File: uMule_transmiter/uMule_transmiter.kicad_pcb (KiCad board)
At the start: 2 copper layers, 61 x 69.9 mm, 73 parts, among them J1 Screw_Terminal_01x02, J2 Conn_01x01_Socket, J3 Screw_Terminal_01x02, J4 Conn_01x01_Socket, J5 Test_Point_Sin_I, J6 Test_Point_Sin_O, J7 Test_Point_Cos_I, J8 Test_Point_Cos_O, J9 Screw_Terminal_01x02, U1 TPS61042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

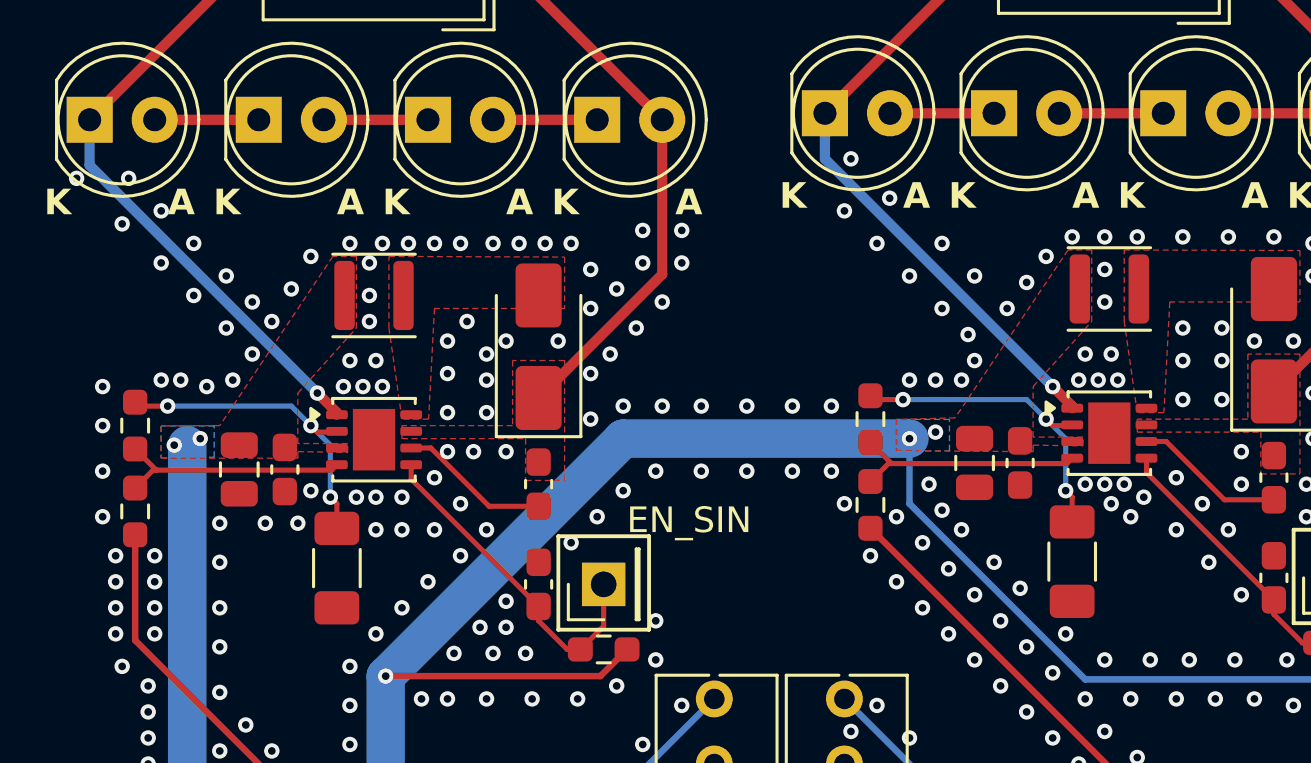
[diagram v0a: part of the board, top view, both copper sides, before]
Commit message: JLC Ready, now waiting for shipment
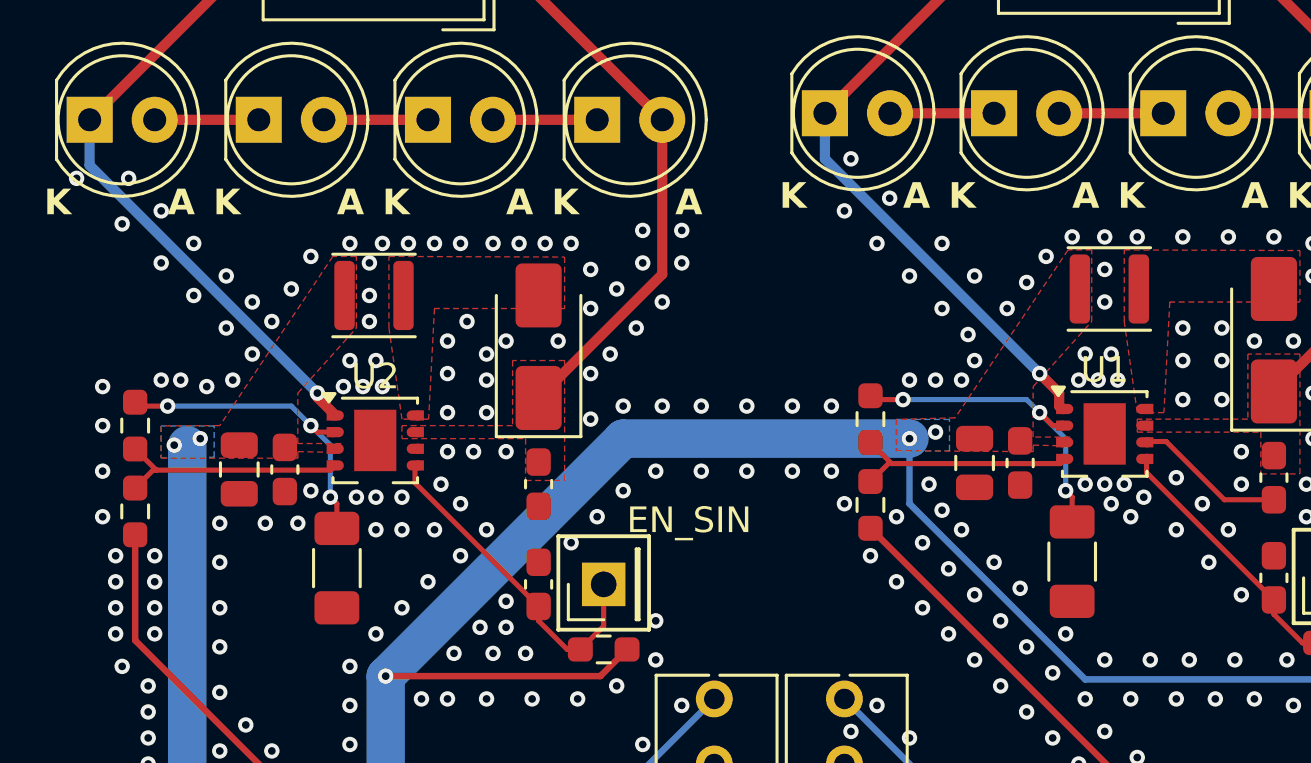
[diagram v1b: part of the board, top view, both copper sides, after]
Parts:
- U1, U2: footprint Package_SON:VSON-8-1EP_3x3mm_P0.65mm_EP1.65x2.4mm -> Package_SON:Texas_S-PVSON-N8
- moved U1 0.18 mm to (172.2, 96.1)
- moved U2 0.06 mm to (143.7, 96.3)
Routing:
- net GND: track 18.7 -> 12.7 mm
